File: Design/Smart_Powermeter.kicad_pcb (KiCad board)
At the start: 2 copper layers, 92 x 87 mm, 147 parts, among them J1 Audio Jack 3P, J2 Audio Jack 3P, J3 Audio Jack 3P, J4 Audio Jack 3P, J5 Audio Jack 3P, J6 Audio Jack 3P, P1 WJ300V-5_0-2P, P2 WJ300V-5_0-3P, Q1 LBSS84LT1G, U1 TYPE-C_16PIN_2MD(073), U2 ESP32-S2-MINI-2-N4R2, U3 AMS1117-3.3, U4 FPC-05FB-24PH20, U5 LM358_C18164495, U6 LM358_C18164495, U7 LM358_C18164495

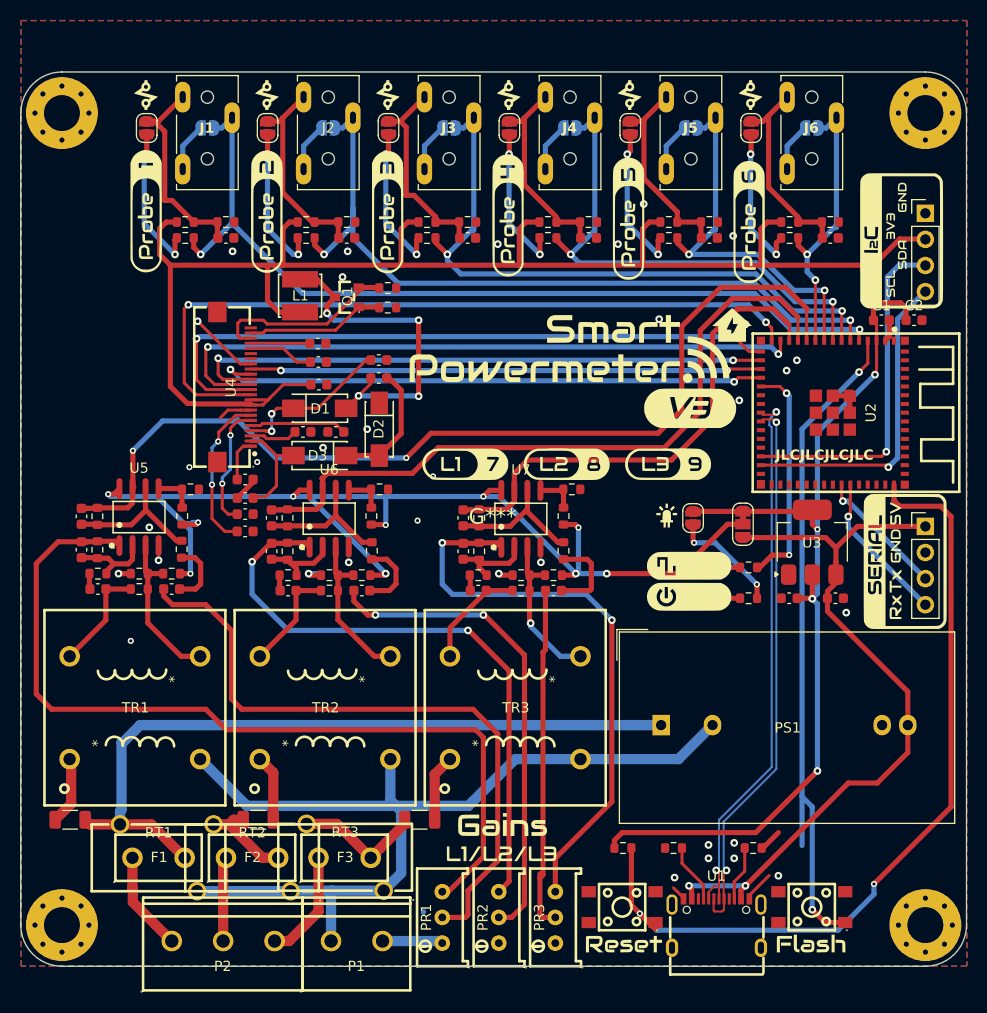
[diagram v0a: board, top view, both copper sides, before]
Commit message: Cleared path around antenna and removed Serial port
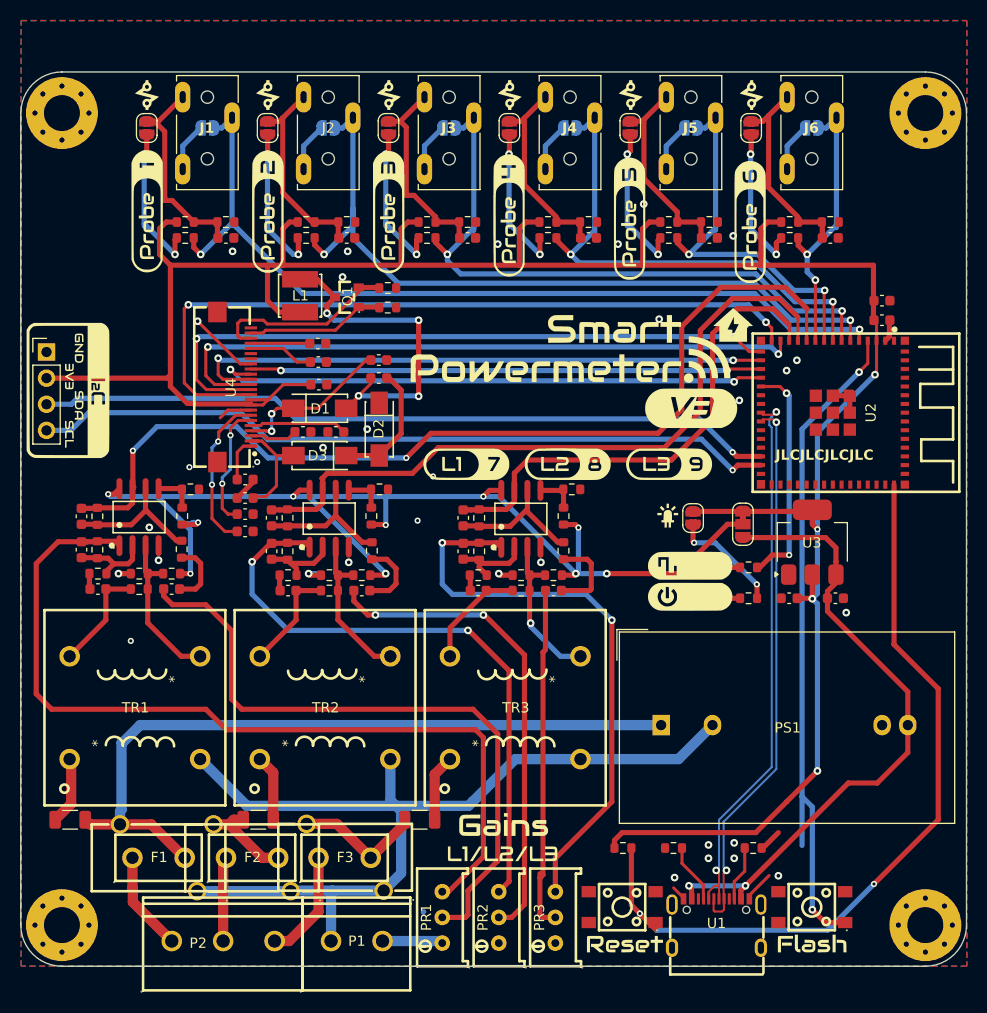
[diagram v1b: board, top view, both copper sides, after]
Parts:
- removed the G*** at (143.4, 101.0)
- removed PH1: Conn_01x04_MountingPin, Connector_PinHeader_2.54mm:PinHeader_1x04_P2.54mm_Vertical
- added ?: LOGO, LOGO, F.Cu at (143.5, 101.0)
- moved PH2 86.6 mm to (100.0, 85.0)
- moved C2 3.66 mm to (181.3, 80.0)
- moved C1 0.05 mm to (181.3, 81.9)
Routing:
- net SCL: track 31.1 -> 72.8 mm
- net SDA: track 33.6 -> 72.1 mm
- net RX: track 14.9 -> 0.00 mm, vias 1 -> 0
- net TX: track 12.8 -> 0.00 mm, vias 1 -> 0
- net +5V: track 72.5 -> 63.0 mm
- net RST: track 81.4 -> 77.4 mm
- net +3.3V: track 243.4 -> 244.9 mm
- net V1: track 94.5 -> 93.9 mm
